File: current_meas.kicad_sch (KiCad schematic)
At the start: 33 parts, among them U23 LT3060ETS8-5#TRMPBF, U24 INA180A2IDBVR, U25 INA180A2IDBVR

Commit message: - zero origin on so - silk - sch trig and rtsi lines need 510 resistor - assembly updated - sch and pcb project name and rev - no changes to gerber, old one can be used
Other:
- title: EOL ECU POWER CARD -> EOL ECU MIX CARD
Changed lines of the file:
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@@
   (paper "A3")
   (title_block
-    (title "EOL ECU POWER CARD")
-    (date "2023-04-03")
-    (rev "0B")
+    (title "EOL ECU MIX CARD")
+    (date "2023-09-26")
+    (rev "0C")
     (company "ARXTRON TECHNOLOGIES")
     (comment 1 "A0180-V0")

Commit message: pnp added
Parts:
- C49, C56, R20, R278: now left out of the parts list

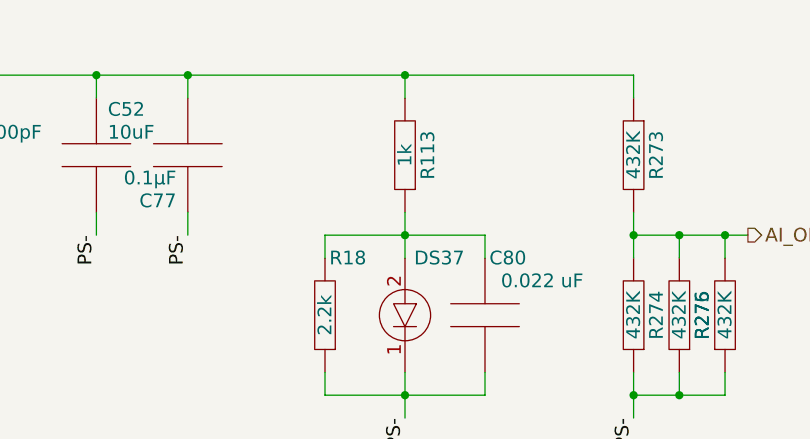
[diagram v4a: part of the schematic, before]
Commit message: dnp res for di pwr dnp led feed for 5v replace with 6.49k feed for ign_on on sim circuit
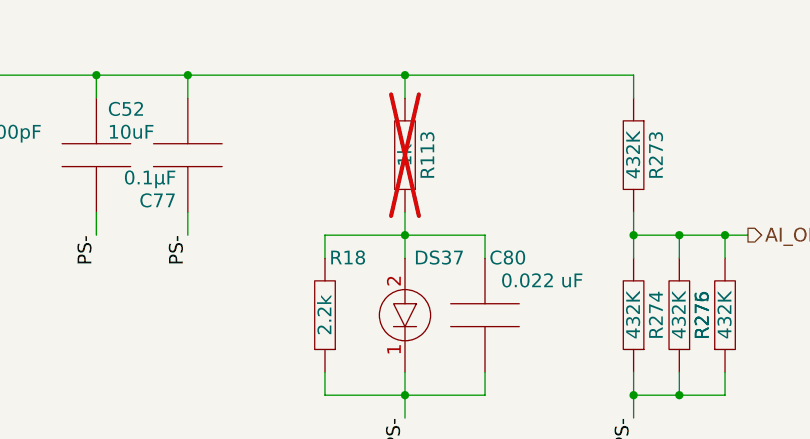
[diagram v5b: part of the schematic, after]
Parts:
- R113: now not fitted; now left out of the parts list
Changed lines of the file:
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@@
   )
   (symbol (lib_id "Resistor_Yageo:RC1206FR-071KL") (at 242.57 50.8 270) (mirror x) (unit 1)
-    (exclude_from_sim no) (in_bom yes) (on_board yes) (dnp no)
+    (exclude_from_sim no) (in_bom no) (on_board yes) (dnp yes)
     (property "Reference" "R113" (at 245.11 50.8 0)
       (effects (font (size 1.524 1.524)))
